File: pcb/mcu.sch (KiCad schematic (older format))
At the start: 14 parts, among them J2 CONN_INTEGRALSTICK_MCU_DEVICE, U1 STM32F777NIH6‎, U10 DSC6083MI2A-032K768, U11 DSC6001HI2A-025.0000‎, U2 XC7A50T-1FTG256C, U6 S25FL064LABNFI011‎

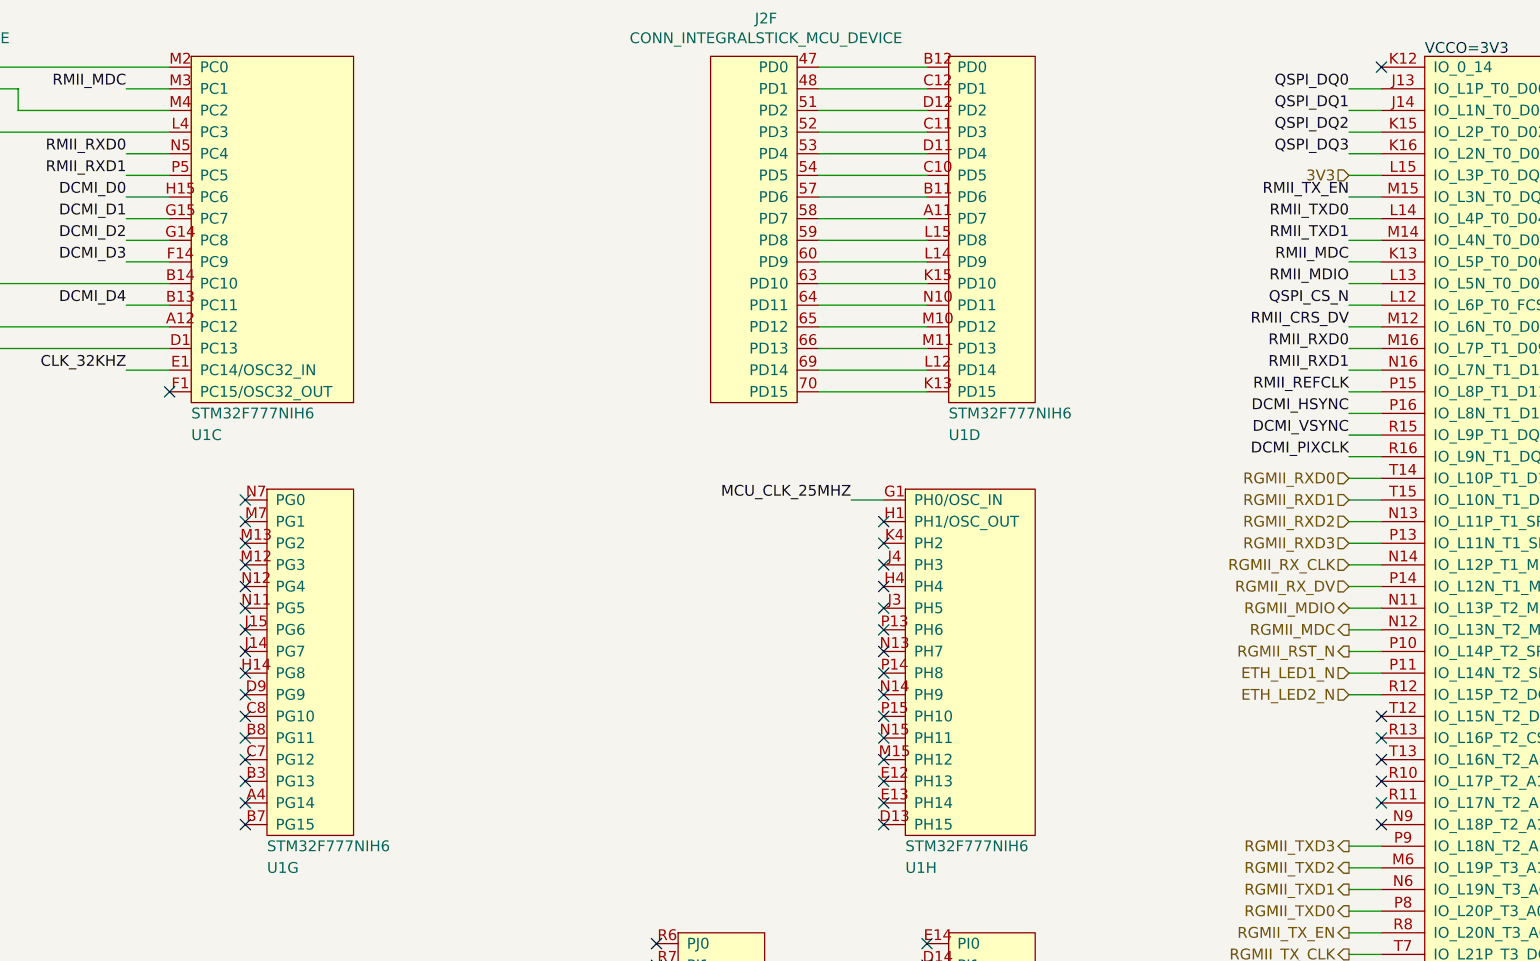
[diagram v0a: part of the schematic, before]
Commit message: Finished initial schematic. Pin assignments will likely change during routing. Ready for test point insertion and signoff review.
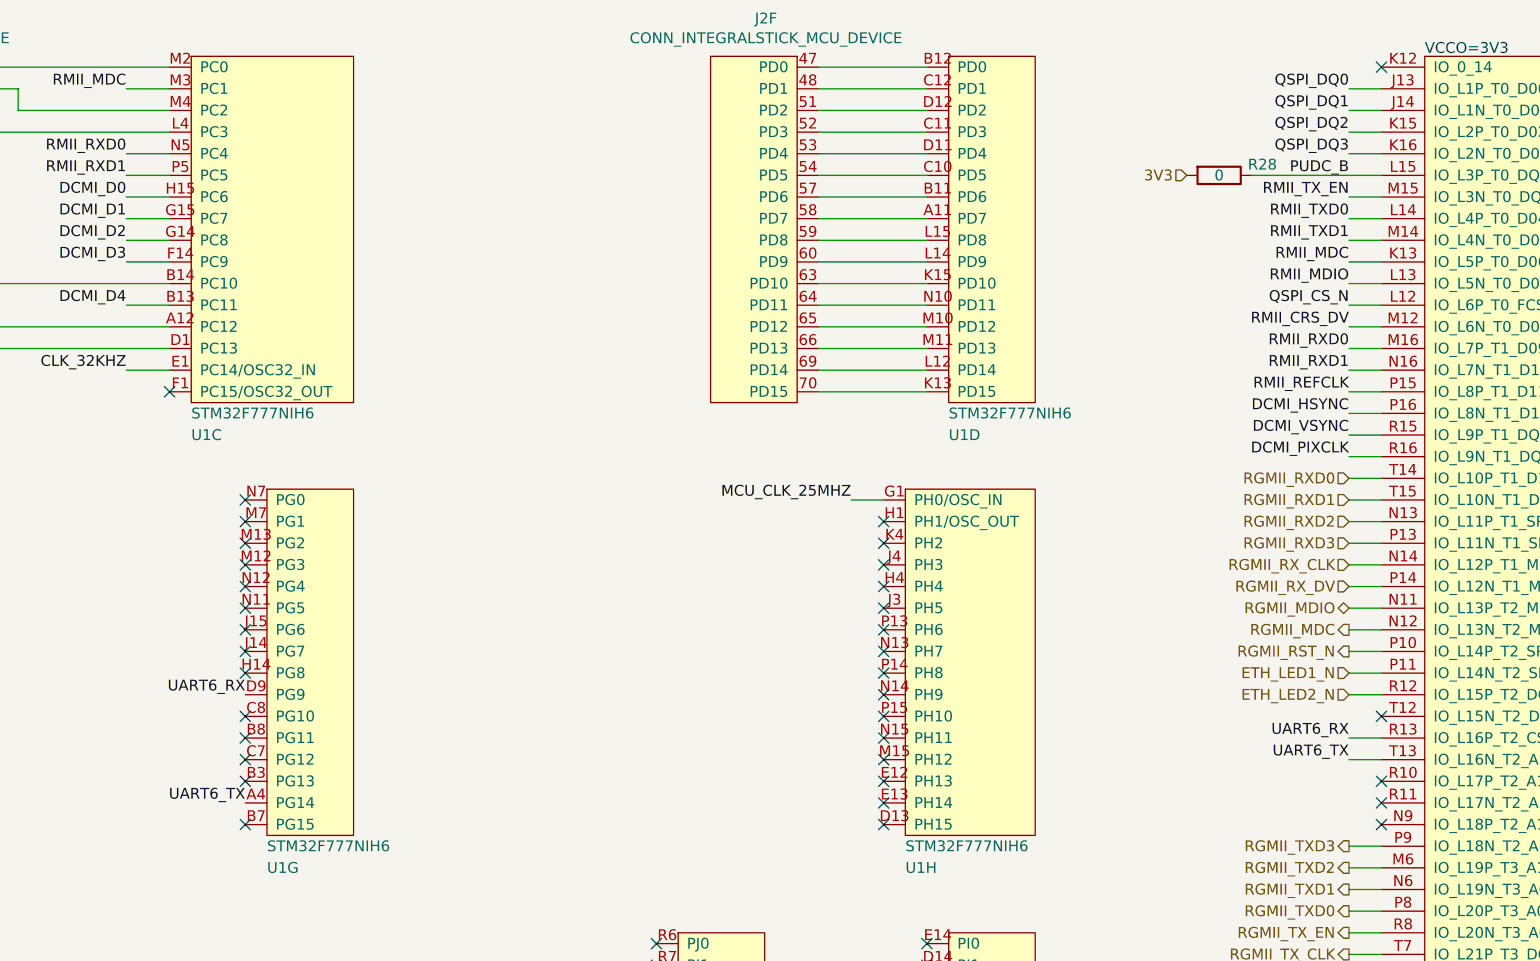
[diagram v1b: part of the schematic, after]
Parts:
- added R28: 0, symbol device:R
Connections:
- net 3V3: now also R28.2; no longer U2.L15 (IO_L3P_T0_DQS_PUDC_B_14)
- net UART6_TX: now reaches U1.A4 (PG14)
- net UART6_TX: now also U2.T13 (IO_L16N_T2_A15_D31_14)
- net UART6_RX: now reaches U1.D9 (PG9)
- net UART6_RX: now also U2.R13 (IO_L16P_T2_CSI_B_14)
- new net PUDC_B: R28.1, U2.L15 (IO_L3P_T0_DQS_PUDC_B_14)
- no-connect marks 85 -> 81
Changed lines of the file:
@@
 $Descr A3 16535 11693
 encoding utf-8
-Sheet 7 7
+Sheet 8 8
 Title "INTEGRALSTICK Compute Module"
-Date "2018-11-06"
+Date "2018-11-07"
 Rev "0.1"
 Comp "Andrew D. Zonenberg"
@@
 Wire Wire Line
 	14100 950  13950 950
-Wire Wire Line
-	13950 1350 14100 1350
 Text Label 13950 1950 2    50   ~ 0
 QSPI_CS_N
@@
 	13950 3550 14100 3550
 NoConn ~ 14100 3850
-NoConn ~ 14100 3950
-NoConn ~ 14100 4050
 NoConn ~ 14100 4250
 NoConn ~ 14100 4350
@@
 NoConn ~ 6150 4350
 NoConn ~ 8850 4350
-NoConn ~ 8850 4250
 NoConn ~ 8850 4150
 NoConn ~ 8850 4050
 NoConn ~ 8850 3950
 NoConn ~ 8850 3850
-NoConn ~ 8850 3750
 NoConn ~ 8850 3650
 NoConn ~ 8850 3550
@@
 Text HLabel 13950 3750 0    50   Input ~ 0
 ETH_LED2_N
-Text HLabel 13950 1350 0    50   Input ~ 0
+Text HLabel 13200 1350 0    50   Input ~ 0
 3V3
 Text HLabel 1350 10450 0    50   Input ~ 0
@@
 QSPI_CLK
 NoConn ~ 14100 4150
+$Comp
+L device:R R28
+U 1 1 5C76D1A0
+P 13350 1350
+F 0 "R28" V 13300 1550 50  0000 C CNN
+F 1 "0" V 13350 1350 50  0000 C CNN
+F 2 "" V 13280 1350 50  0001 C CNN
+F 3 "" H 13350 1350 50  0001 C CNN
+	1    13350 1350
+	0    1    1    0
+$EndComp
+Text Label 13950 1350 2    50   ~ 0
+PUDC_B
+Wire Wire Line
+	13500 1350 14100 1350
+Text Label 8850 3750 2    50   ~ 0
+UART6_RX
+Text Label 8850 4250 2    50   ~ 0
+UART6_TX
+Text Label 13950 3950 2    50   ~ 0
+UART6_RX
+Text Label 13950 4050 2    50   ~ 0
+UART6_TX
+Wire Wire Line
+	14100 3950 13950 3950
+Wire Wire Line
+	13950 4050 14100 4050
 $EndSCHEMATC

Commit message: Added capacitor for bbRAM on STM32. Removed MCU config oscillator, we now use the FPGA or internal oscillator as clock. Added SPI bus from FPGA to MCU.
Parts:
- removed C46: 0.47 uF, symbol device:C
- removed U11: DSC6001HI2A-025.0000‎, symbol osc-azonenberg:OSC
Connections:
- net MCU_CLK_25MHZ: now also R22.2; no longer R22.1
- net SPI5_MOSI: now reaches U1.P8 (PF11)
- net SPI5_MOSI: now also U2.K12 (IO_0_14)
- net SPI5_CS_N: now reaches U1.J3 (PH5)
- net SPI5_CS_N: now also U2.T12 (IO_L15N_T2_DQS_DOUT_CSO_B_14)
- net SPI5_MISO: now reaches U1.N13 (PH7)
- net SPI5_MISO: now also U2.N9 (IO_L18P_T2_A12_D28_14)
- net SPI5_SCK: now reaches U1.P13 (PH6)
- net SPI5_SCK: now also U2.R11 (IO_L17N_T2_A13_D29_14)
- net at U2.R10 (IO_L17P_T2_A14_D30_14): now also R22.1
- no-connect marks 81 -> 72
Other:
- moved on the sheet: R22
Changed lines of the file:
@@
 Wire Wire Line
 	13950 3550 14100 3550
-NoConn ~ 14100 3850
-NoConn ~ 14100 4250
-NoConn ~ 14100 4350
 $Comp
 L st-azonenberg:STM32F777xx-TFBGA216 U?
@@
 	5000 3750 6150 3750
 NoConn ~ 6150 3850
-NoConn ~ 6150 3950
 NoConn ~ 6150 4050
 NoConn ~ 6150 4150
@@
 NoConn ~ 11800 3050
 NoConn ~ 11800 3150
-NoConn ~ 11800 3250
-NoConn ~ 11800 3350
-NoConn ~ 11800 3450
-NoConn ~ 11800 3550
 NoConn ~ 11800 3650
 NoConn ~ 11800 3750
@@
 NoConn ~ 10750 5000
 NoConn ~ 10750 4900
-NoConn ~ 14100 850
 Wire Wire Line
 	13950 3650 14100 3650
@@
 NoConn ~ 8500 2350
 $Comp
-L osc-azonenberg:OSC U11
-U 1 1 5BEE00E3
-P 2150 9100
-F 0 "U11" H 2125 9387 60  0000 C CNN
-F 1 "DSC6001HI2A-025.0000‎" H 2125 9281 60  0000 C CNN
-F 2 "" H 2150 9100 60  0000 C CNN
-F 3 "" H 2150 9100 60  0000 C CNN
-	1    2150 9100
-	1    0    0    -1
-$EndComp
-Text Label 1300 9100 2    50   ~ 0
-3V3
-Wire Wire Line
-	1300 9100 1350 9100
-Wire Wire Line
-	1350 9100 1350 9200
-Wire Wire Line
-	1350 9200 1450 9200
-Connection ~ 1350 9100
-Wire Wire Line
-	1350 9100 1450 9100
-Text Label 1300 9300 2    50   ~ 0
-GND
-$Comp
 L device:R R22
 U 1 1 5BEE00F4
-P 3050 9100
-F 0 "R22" V 2950 9000 50  0000 C CNN
-F 1 "33" V 3050 9100 50  0000 C CNN
-F 2 "" V 2980 9100 50  0001 C CNN
-F 3 "" H 3050 9100 50  0001 C CNN
-	1    3050 9100
+P 13800 4150
+F 0 "R22" V 13750 4350 50  0000 C CNN
+F 1 "33" V 13800 4150 50  0000 C CNN
+F 2 "" V 13730 4150 50  0001 C CNN
+F 3 "" H 13800 4150 50  0001 C CNN
+	1    13800 4150
 	0    1    1    0
 $EndComp
-Wire Wire Line
-	2900 9100 2800 9100
-Text Label 3200 9100 0    50   ~ 0
+Text Label 13650 4150 2    50   ~ 0
 MCU_CLK_25MHZ
-$Comp
-L device:C C46
-U 1 1 5BEE0100
-P 700 9150
-F 0 "C46" H 815 9196 50  0000 L CNN
-F 1 "0.47 uF" H 815 9105 50  0000 L CNN
-F 2 "" H 738 9000 50  0001 C CNN
-F 3 "" H 700 9150 50  0001 C CNN
-	1    700  9150
-	1    0    0    -1
-$EndComp
-Wire Wire Line
-	700  9300 1450 9300
-Wire Wire Line
-	700  9000 1350 9000
-Wire Wire Line
-	1350 9000 1350 9100
 Text Label 11650 2850 2    50   ~ 0
 MCU_CLK_25MHZ
@@
 Text HLabel 3150 10350 2    50   Input ~ 0
 QSPI_CLK
-NoConn ~ 14100 4150
 $Comp
 L device:R R28
@@
 Wire Wire Line
 	13950 4050 14100 4050
+Wire Wire Line
+	14100 4150 13950 4150
+Wire Wire Line
+	11650 3350 11800 3350
+NoConn ~ 11800 3250
+Wire Wire Line
+	11650 3450 11800 3450
+Wire Wire Line
+	11650 3550 11800 3550
+Text Label 11650 3350 2    50   ~ 0
+SPI5_CS_N
+Text Label 11650 3450 2    50   ~ 0
+SPI5_SCK
+Text Label 11650 3550 2    50   ~ 0
+SPI5_MISO
+Text Label 6150 3950 2    50   ~ 0
+SPI5_MOSI
+Text Label 13950 850  2    50   ~ 0
+SPI5_MOSI
+Wire Wire Line
+	14100 850  13950 850
+Text Label 13950 3850 2    50   ~ 0
+SPI5_CS_N
+Text Label 13950 4250 2    50   ~ 0
+SPI5_SCK
+Text Label 13950 4350 2    50   ~ 0
+SPI5_MISO
+Wire Wire Line
+	13950 3850 14100 3850
+Wire Wire Line
+	13950 4250 14100 4250
+Wire Wire Line
+	13950 4350 14100 4350
 $EndSCHEMATC
